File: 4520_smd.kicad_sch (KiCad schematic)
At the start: 4 parts, among them U8 4017

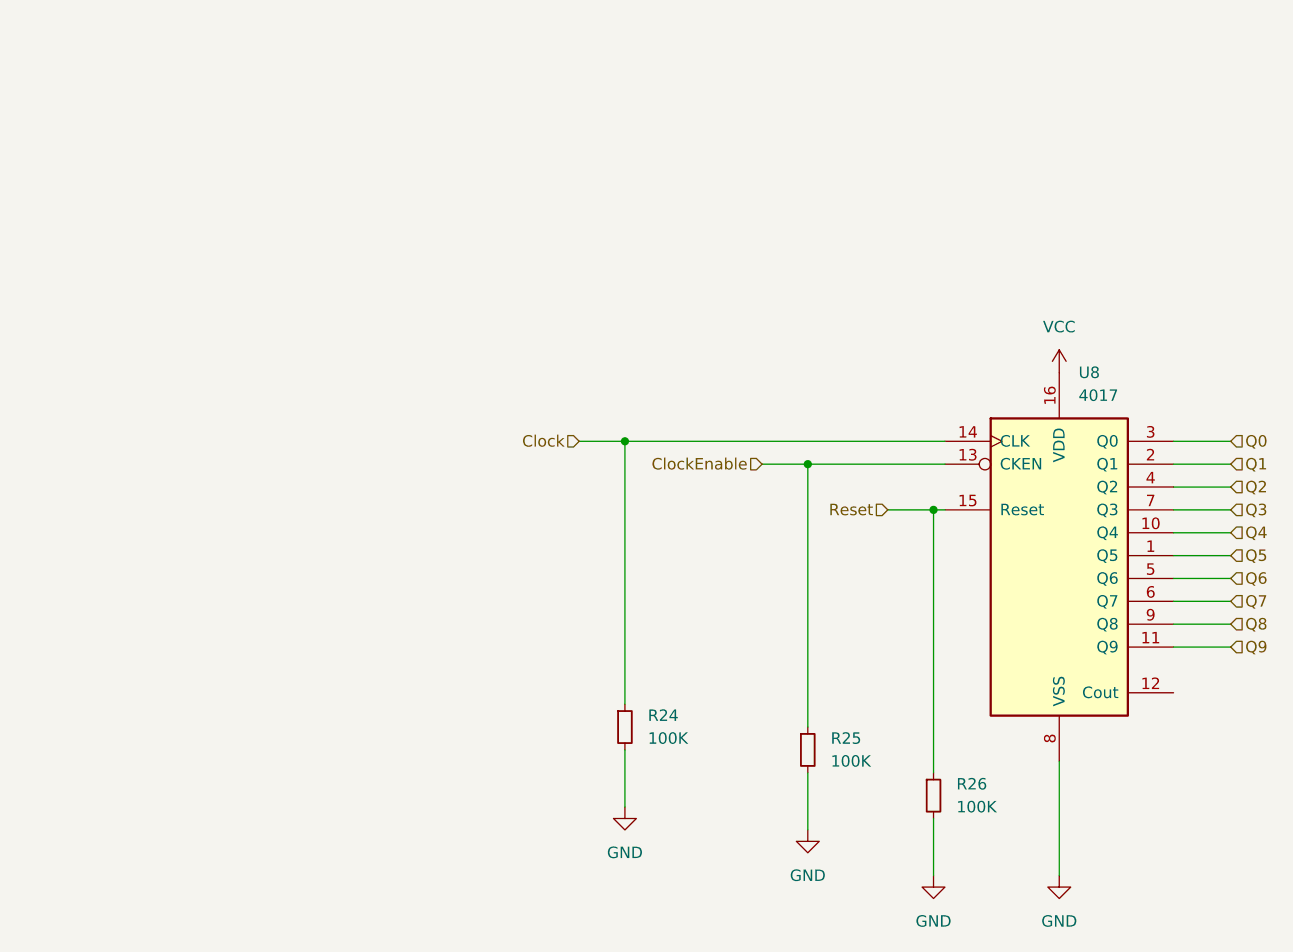
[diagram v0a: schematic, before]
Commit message: start smd refactoring
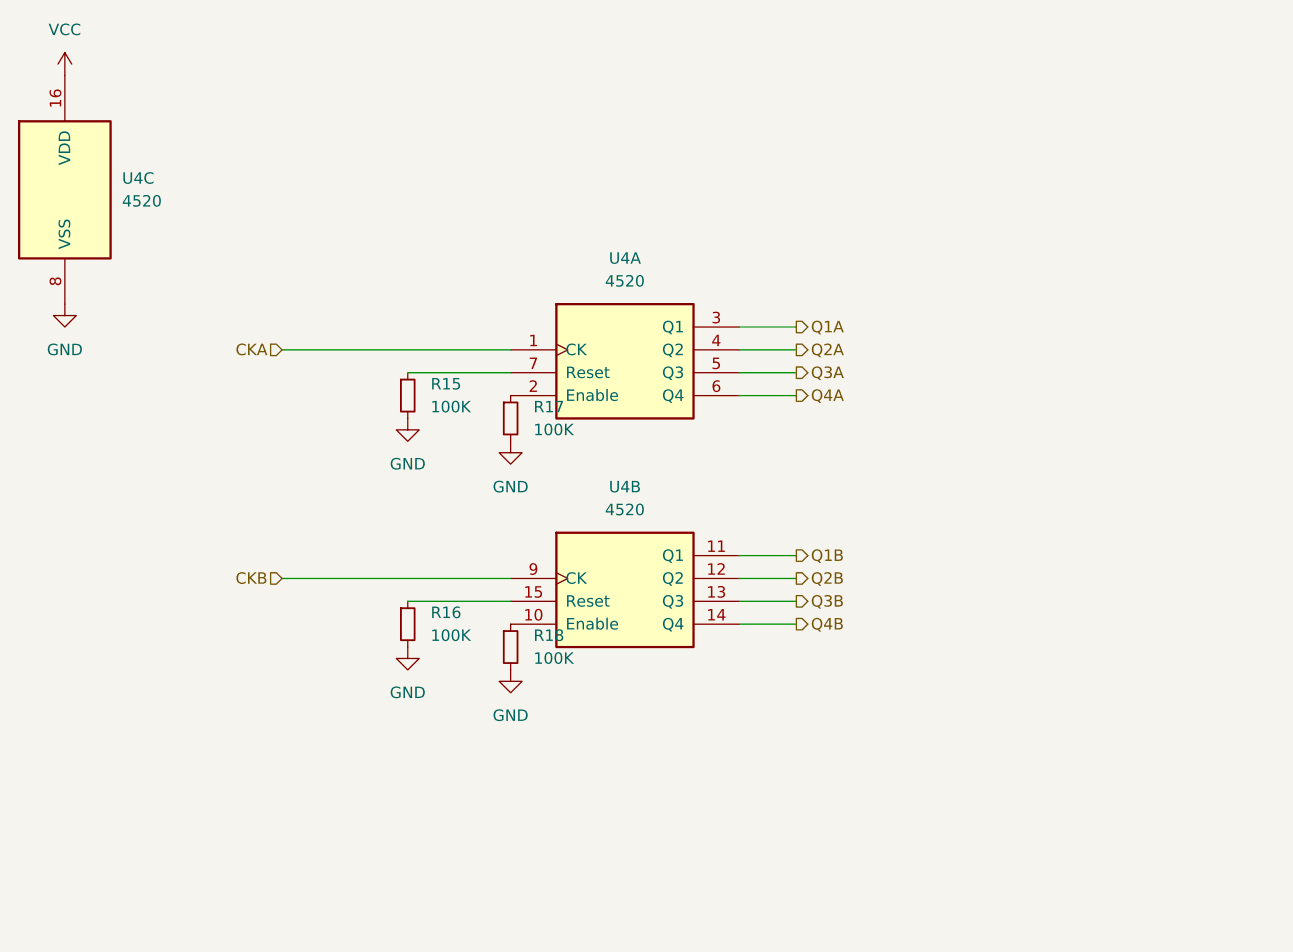
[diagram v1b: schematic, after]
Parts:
- removed R24, R25, R26: 100K, R_0805_2012Metric, symbol Device:R_Small
- removed U8: 4017, SOIC-16_3.9x9.9mm_P1.27mm, symbol 4xxx:4017
- added R15, R16, R17, R18: 100K, Resistor_THT:R_Axial_DIN0207_L6.3mm_D2.5mm_P10.16mm_Horizontal, symbol Device:R_Small
- added U4: 4520, Package_SO:SO-16_5.3x10.2mm_P1.27mm, symbol 4xxx:4520
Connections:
- net GND: now also R15.2, R16.2, R17.2, R18.2, U4.8 (VSS)
- net VCC: now also U4.16 (VDD)
- new net: R16.1, U4.15 (Reset)
- new net: R15.1, U4.7 (Reset)
- new net: R18.1, U4.10 (Enable)
- new net: R17.1, U4.2 (Enable)
- new net CKA: U4.1 (CK)
- new net CKB: U4.9 (CK)
- new net Q1A: U4.3 (Q1)
- new net Q1B: U4.11 (Q1)
- new net Q2A: U4.4 (Q2)
- new net Q2B: U4.12 (Q2)
- new net Q3A: U4.5 (Q3)
- new net Q3B: U4.13 (Q3)
- new net Q4A: U4.6 (Q4)
- new net Q4B: U4.14 (Q4)
